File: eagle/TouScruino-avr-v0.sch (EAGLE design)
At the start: 43 parts, among them Q1 8MHz, Q2 MMBT2222A, Q3 8MHz, Q4 8MHz, U1 uSD-SOCKET, U2 PJ28004C, U3 ARDUINO_SHIELD, U4 MCP73831, U5 MIC5209-3.3YS, X1 USBSMD

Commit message: 
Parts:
- removed Q4: 8MHz, wibauxl:CRYSTAL_5X3.2
- removed S2: SWITCH-MOMENTARY-2SMD, SparkFun:SWITCH-MOMENTARY-2SMD
- removed U2: PJ28004C, wibauxl:PJ28004C
- removed X1: USBSMD, SparkFun:USBSMD
- added C12: 10nF, SparkFun:CAP0805
- added C13: 100nF, SparkFun:CAP0805
- added C14: 10uF, SparkFun:CAP0805
- added C3: 0.1uF, SparkFun:CAP0805
- added D1: BAT54C, wibauxl:BAT54C
- added J1: AVR_ISP, SparkFun:AVR_SPI_PRG_6PTH
- added R10: 4K7, SparkFun:RESISTOR0805-RES
- added R9: 4k7, SparkFun:RESISTOR0805-RES
- added SJ2: SJ_2WAYS_1-2, wibauxl:SJ_2WAYS_1-2
- added SJ4, SJ5: SOLDERJUMPERTRACE, SparkFun:SOLDERJUMPERTRACE
- added X2: USB-MICROB, SparkFun:USB-MICROB
- C11: value 18pF -> 10nF; device SparkFun:CAP0603-CAP -> SparkFun:CAP0805
- C2: value 18pF -> 0.1uF; device SparkFun:CAP0603-CAP -> SparkFun:CAP0805
- JP1: value M20 -> (none); device SparkFun:M20 -> SparkFun:ARDUINO_SERIAL_PROGRAMPTH
- R2: value 10k -> 10K
- R4: value 20k -> 75K
- R7: value 22 -> 20k
- U$6: value ATSAM3S_C -> TFT_20; device wibauxl:ATSAM3S_C -> wibauxl:TFT_20
- U1: value uSD-SOCKET -> ATMEGA1284P; device SparkFun:USD-SOCKETNEW -> wibauxl:ATMEGA324A
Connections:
- removed net A.A0: U$6.PA17/AD0, U3.A0
- removed net A.A1: U$6.PB0/AD4, U3.A1
- removed net A.A2: U$6.PB1/AD5, U3.A2
- removed net A.A3: U$6.PB2/AD6, U3.A3
- removed net A.A4: U$6.PB3/AD7, U3.A4
- removed net A.A5: U$6.PC12/NCS3/AD12, U3.A5
- removed net A.AREF: U$6.ADVREF, U3.AREF
- removed net A.D0/RX0: U$6.PA21/RXD1/AD8, U3.RX
- removed net A.D1/TX0: U$6.PA22/TXD1/AD9, U3.TX
- removed net A.D10: U$6.PA11/NPCS0, U3.D10
- removed net A.D11/MISO: U$4.SDO/IRQ, U$6.PA12/MISO, U3.D11
- removed net A.D12/MOSI: U$4.SDI/SDA, U$6.PA13/MOSI, U3.D12
- removed net A.D13: U3.D13
- removed net A.D13/SCK: R5.2, U$4.SCK/SCL, U$6.PA14/SCK
- removed net A.D2/RX1: U$6.PA9/URXD0, U3.D2
- removed net A.D3/TX1: U$6.PA10/UTXD0, U3.D3
- removed net A.D4: U$6.PA24/A20, U3.D4
- removed net A.D5: U$6.PC13/AD10, U3.D5
- removed net A.D6: U$6.PA15/TIOA1, U3.D6
- removed net A.D7/DAC0: U$6.PB13/DAC0, U3.D7
- removed net A.D8/DAC1: U$6.PB14/DAC1, U3.D8
- removed net A.D9: U$6.PA16/TIOB1, U3.D9
- removed net A.SCL: JP3.1, U$6.PA4/SCL0
- removed net A.SDA: JP3.2, U$6.PA3/SDA0
- removed net A0: U$6.PC18/A0
- removed net A1: U$6.PC19/A1, U2.DC
- removed net A10: U$6.PC28/A10
- removed net A11: U$6.PC29/A11
- removed net A12: U$6.PC30/A12
- removed net A13: U$6.PC31/A13
- removed net A14: U$6.PA18/A14/AD1
- removed net A15: U$6.PA19/A15/AD2
- removed net A16: U$6.PA20/A16/AD3
- removed net A17: U$6.PA0/A17
- removed net A18: U$6.PA1/A18
- removed net A19: U$6.PA23/A19
- removed net A2: U$6.PC20/A2
- removed net A21: U$6.PC16/A21
- removed net A22: U$6.PC17/A22
- removed net A3: U$6.PC21/A3
- removed net A4: U$6.PC22/A4
- removed net A5: U$6.PC23/A5
- removed net A6: U$6.PC24/A6
- removed net A7: U$6.PC25/A7
- removed net A8: U$6.PC26/A8
- removed net A9: U$6.PC27/A9
- removed net D0: U$6.PC0/D0, U2.DB0
- removed net D1: U$6.PC1/D1, U2.DB1
- removed net D2: U$6.PC2/D2, U2.DB2
- removed net D3: U$6.PC3/D3, U2.DB3
- removed net D5: U$6.PC5/D5, U2.DB5
- removed net D6: U$6.PC6/D6, U2.DB6
- removed net LCD.BL: U$6.PA2/PWMH2
- removed net LCD_CS: U$6.PC15/NCS1/AD11, U2.CS
- removed net N$14: S2.2, U$6.ERASE/PB12
- removed net N$25: R7.1, U2.LEDK3, U2.LEDK4
- removed net N$32: R6.1, U2.LEDK1, U2.LEDK2
- removed net N$45: C2.1, Q4.1, U$6.PA7/XIN32
- removed net N$46: C11.1, Q4.2, U$6.PA8/XOUT32
- removed net PD_CS: U$6.PC14/NCS0
- removed net RD: U$6.PC11/NRD, U2.RD
- removed net SD.CD: U$6.PA25/A23, U1.SHIELD@2
- removed net SD.CLK: U$6.PA29/MCCCK, U1.SCK
- removed net SD.CMD: U$6.PA28/MCCDA, U1.DI
- removed net SD.D0: U$6.PA30/MCDA0, U1.DO
- removed net SD.D1: U$6.PA31/MCDA1, U1.RSV
- removed net SD.D2: U$6.PA26/MCDA2, U1.NC
- removed net SD.D3: U$6.PA27/MCDA3, U1.CS
- removed net TCK: U$6.TCK/PB7
- removed net TDI: U$6.TDI/PB4
- removed net TDO: U$6.TDO/PB5
- removed net TMS: U$6.TMS/PB6
- removed net TS.CS: U$4.SS, U$6.PA5/NPCS3
- removed net TS.IRQ: U$4.SIQ, U$6.PA6
- removed net USB.D+: U$6.DDP/PB11, X1.D+
- removed net USB.D-: U$6.DDM/PB10, X1.D-
- removed net WR: U$6.PC8/NWE, U2.WR
- new net A0/D24: U1.(PCINT0/ADC0)PA0, U3.A0
- new net A1/D25: U1.(PCINT1/ADC1)PA1, U3.A1
- new net A2/D26: U1.(PCINT2/ADC2)PA2, U3.A2
- new net A3/D27: U1.(PCINT3/ADC3)PA3, U3.A3
- new net A4/D28: U1.(PCINT4/ADC4)PA4, U3.A4
- new net A5/D29: U1.(PCINT5/ADC5)PA5, U3.A5
- new net A6/D30: U$4.SDO/IRQ, U1.(PCINT6/ADC6)PA6
- new net A7/D31: U$6.DC, U1.(PCINT7/ADC7)PA7
- new net AREF: C1.2, U1.AREF, U3.AREF
- new net D0/RX: JP1.TXO, U1.(PCINT24/RXD0)PD0, U3.RX
- new net D1/TX: JP1.RXI, U1.(PCINT25/TXD0)PD1, U3.TX
- new net D10/PWM4: U1.(PCINT31/OC2A)PD7, U3.D10
- new net D11/MOSI: J1.4, SJ4.2, U$6.D5, U1.(PCINT13/MOSI)PB5
- new net D12/MISO: J1.1, U$6.D6, U1.(PCINT14/MISO)PB6, U3.D12
- new net D13/SCK: J1.3, R5.2, SJ5.2, U$6.D7, U1.(PCINT15/SCK)PB7
- new net D14: U$6.D0, U1.(PCINT8/XCK0/T0)PB0
- new net D15: U$6.D1, U1.(PCINT9/CLKO/T1)PB1
- new net D16: U$6.D2, U1.(PCINT10/INT2/AIN0)PB2
- new net D17: U$6.D3, U1.(PCINT11/OC0A/AIN1)PB3
- new net D18: U$6.D4, U1.(PCINT12/OC0B/!SS!)PB4
- new net D19/SCL: JP3.1, R10.1, U$4.SCK/SCL, U1.(PCINT16/SCL)PC0
- new net D2/RX1: U1.(PCINT26/INT0/RXD1)PD2, U3.D2
- new net D20/SDA: JP3.2, R9.1, U$4.SDI/SDA, U1.(PCINT17/SDA)PC1
- new net D21: U$6.CS, U1.(PCINT21/TDI)PC5
- new net D22: D1.A1, U$6.WR, U1.(PCINT22/TOSC1)PC6
- new net D23: D1.A2, U$6.RD, U1.(PCINT23/TOSC2)PC7
- new net D3/TX1: U1.(PCINT27/INT1/TXD1)PD3, U3.D3
- new net D6/PWM2: U1.(PCINT29/OC1A)PD5, U3.D6
- new net D8: U1.(PCINT20/TDO)PC4, U3.D8
- new net D9/PWM3: U1.(PCINT30/OC2B/ICP)PD6, U3.D9
- new net DTR: C2.2, JP1.DTR
- new net LCD_RES: SJ2.2, U$6.RST
- new net N$3: SJ4.1, U3.D11
- new net N$6: R7.1, U$4.WAKE
- net 3.3V: now also C13.2, C14.2, C3.2, J1.2, JP1.VCC, R10.2, R9.2, U$6.VCC, U1.AVCC, U1.VCC@1, U1.VCC@2; no longer C1.2, S2.1, U$4.M1, U$6.VDDIN, U$6.VDDIO@1, U$6.VDDIO@2, U$6.VDDIO@3, U$6.VDDIO@4, U$6.VDDIO@5, U2.LEDA, U2.VCC, U2.VCCIO@1, U2.VCCIO@2
- net D4: now also U1.(PCINT18/TCK)PC2, U3.D4; no longer U$6.PC4/D4, U2.DB4
- net D5/PWM1: now also U1.(PCINT28/OC1B)PD4, U3.D5
- net D7: now also U1.(PCINT19/TMS)PC3, U3.D7; no longer U$6.PC7/D7, U2.DB7
- net GND: now also C11.1, C12.1, C13.1, C14.1, C3.1, J1.6, JP1.CTS, JP1.GND, R4.1, S1.2, U$4.M1, U$4.SS, U$6.GND, U1.GND@1, U1.GND@2, U1.GND@3, X2.GND; no longer C11.2, C2.2, S1.1, U$6.GND@1, U$6.GND@2, U$6.GND@3, U$6.GND@4, U$6.GND@5, U$6.JTAGSEL, U$6.TST, U1.SHIELD@1, U1.SHIELD@3, U2.GND@1, U2.GND@2, X1.GND
- net N$1: now also U1.XTAL1; no longer U$6.XIN/PB9
- net N$10: now also SJ5.1, U3.D13; no longer U$6.VDDCORE@1, U$6.VDDCORE@2, U$6.VDDCORE@3, U$6.VDDCORE@4, U$6.VDDOUT, U$6.VDDPLL
- net N$11: now also R6.1, U$6.BL; no longer R4.2, U$4.WAKE
- net N$2: now also U1.XTAL2; no longer U$6.XOUT/PB8
- net N$7: no longer R7.2
- net N$9: now also D1.K, R4.2, SJ2.1; no longer R2.1, S1.2, U$6.NRST
- net RES: now also C2.1, J1.5, R2.1, S1.1, SJ2.3, U1.RESET
- net VUSB: now also X2.VBUS; no longer X1.VBUS
- net X+: now also U$6.X+; no longer U2.X+
- net X-: now also C11.2, R7.2, U$6.X-; no longer U2.X-
- net Y+: now also U$6.Y+; no longer U2.Y+
- net Y-: now also C12.2, U$6.Y-; no longer R4.1, U2.Y-
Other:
- note added: "Beware: do not connect the two outside pins"
- moved on the sheet: C1, C10, C11, C2, C9, JP4, LED2, Q1, Q2, Q3, R2, R4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

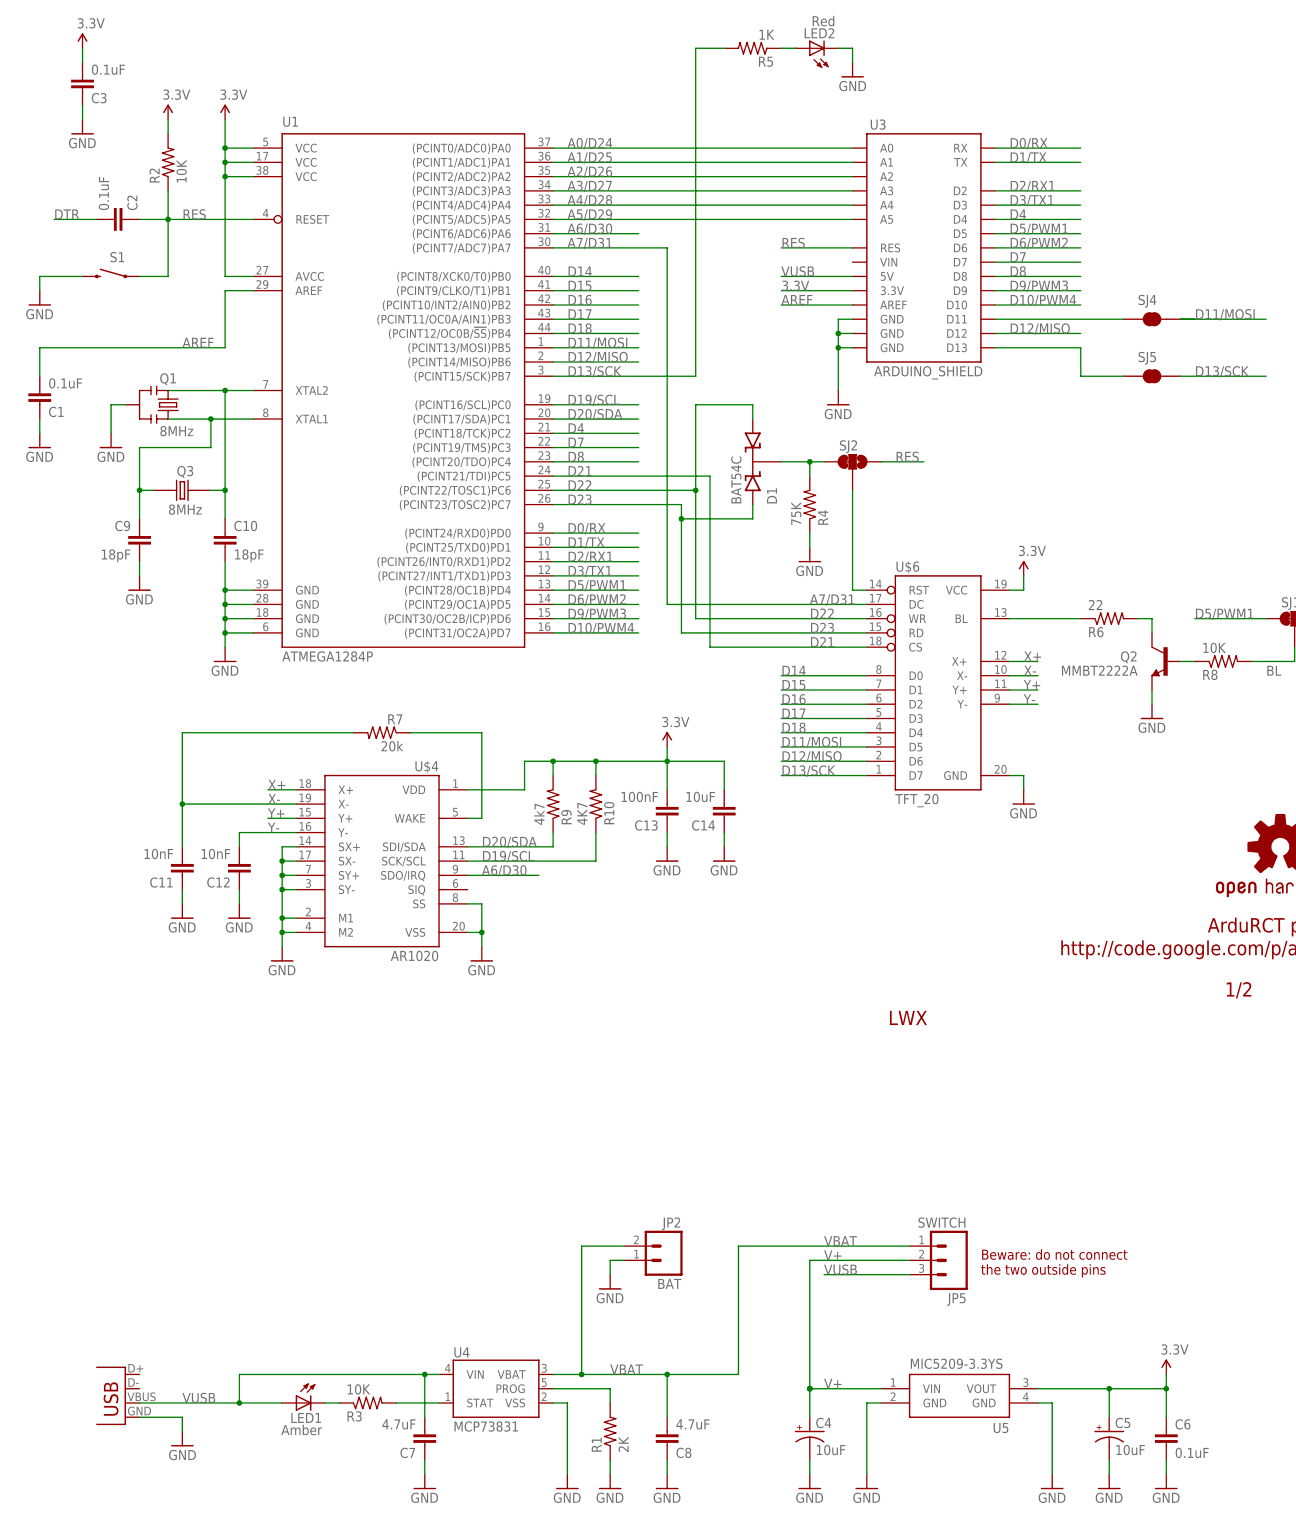
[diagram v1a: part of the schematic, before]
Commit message: 
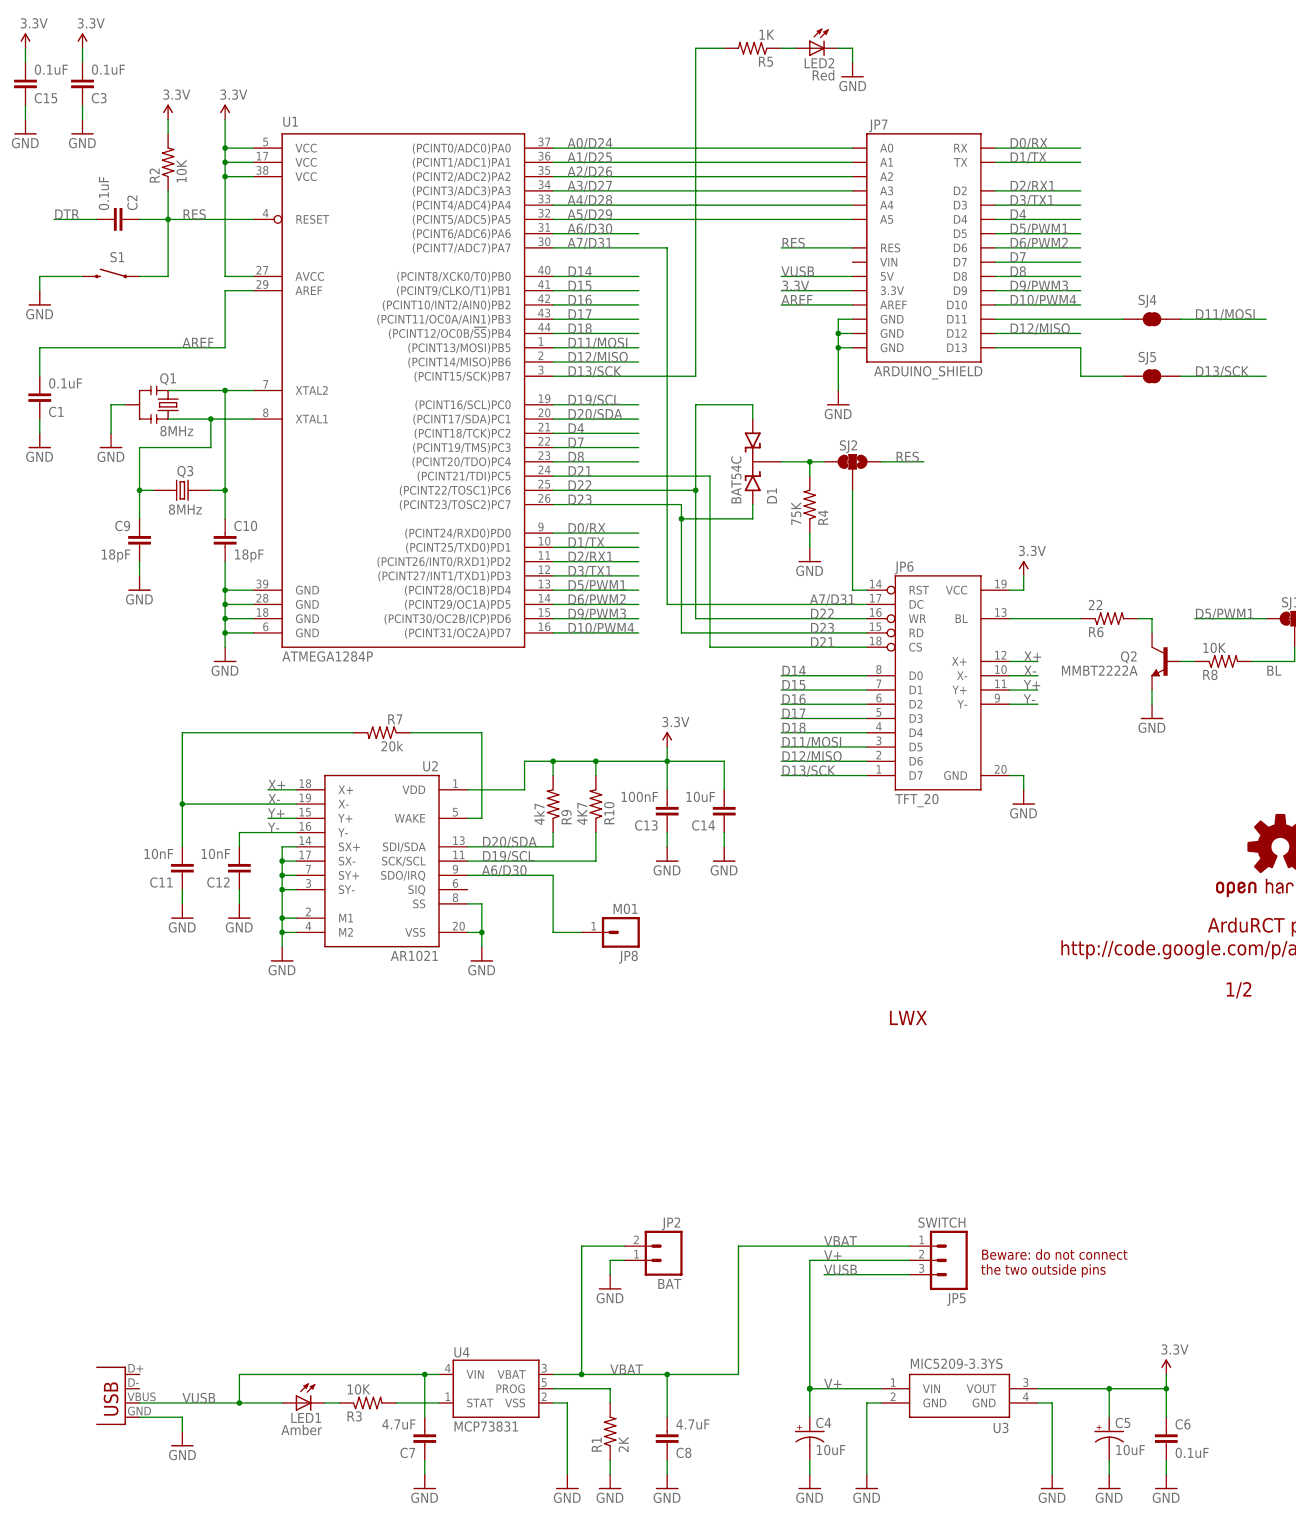
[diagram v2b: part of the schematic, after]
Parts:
- removed U5: MIC5209-3.3YS, wibauxl:MIC5209
- added C15: 0.1uF, SparkFun:CAP0805
- added JP7: ARDUINO_SHIELD, wibauxl:ARDUINO_SHIELD
- added JP8: M01, wibauxl:M01
- LED2: device wibauxl:LED805 -> wibauxl:LED
- U2: value AR1020 -> AR1021
- U3: value ARDUINO_SHIELD -> MIC5209-3.3YS; device wibauxl:ARDUINO_SHIELD -> wibauxl:MIC5209
- renumbered U$4 to U2, U$6 to JP6
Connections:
- net 3.3V: now also C15.2, JP7.3.3V, U3.VOUT; no longer U3.3.3V, U5.VOUT
- net A0/D24: now also JP7.A0; no longer U3.A0
- net A1/D25: now also JP7.A1; no longer U3.A1
- net A2/D26: now also JP7.A2; no longer U3.A2
- net A3/D27: now also JP7.A3; no longer U3.A3
- net A4/D28: now also JP7.A4; no longer U3.A4
- net A5/D29: now also JP7.A5; no longer U3.A5
- net A6/D30: now also JP8.1
- net AREF: now also JP7.AREF; no longer U3.AREF
- net D0/RX: now also JP7.RX; no longer U3.RX
- net D1/TX: now also JP7.TX; no longer U3.TX
- net D10/PWM4: now also JP7.D10; no longer U3.D10
- net D12/MISO: now also JP7.D12; no longer U3.D12
- net D2/RX1: now also JP7.D2; no longer U3.D2
- net D3/TX1: now also JP7.D3; no longer U3.D3
- net D4: now also JP7.D4; no longer U3.D4
- net D5/PWM1: now also JP7.D5; no longer U3.D5
- net D6/PWM2: now also JP7.D6; no longer U3.D6
- net D7: now also JP7.D7; no longer U3.D7
- net D8: now also JP7.D8; no longer U3.D8
- net D9/PWM3: now also JP7.D9; no longer U3.D9
- net GND: now also C15.1, JP7.GND@0, JP7.GND@1, JP7.GND@2; no longer U3.GND@0, U5.GND@1, U5.GND@2
- net N$10: now also JP7.D13; no longer U3.D13
- net N$3: now also JP7.D11; no longer U3.D11
- net RES: now also JP7.RES; no longer U3.RES
- net V+: now also U3.VIN; no longer U5.VIN
- net VUSB: now also JP7.5V; no longer U3.5V
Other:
- moved on the sheet: LED2
